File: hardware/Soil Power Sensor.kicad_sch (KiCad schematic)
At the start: 0 parts

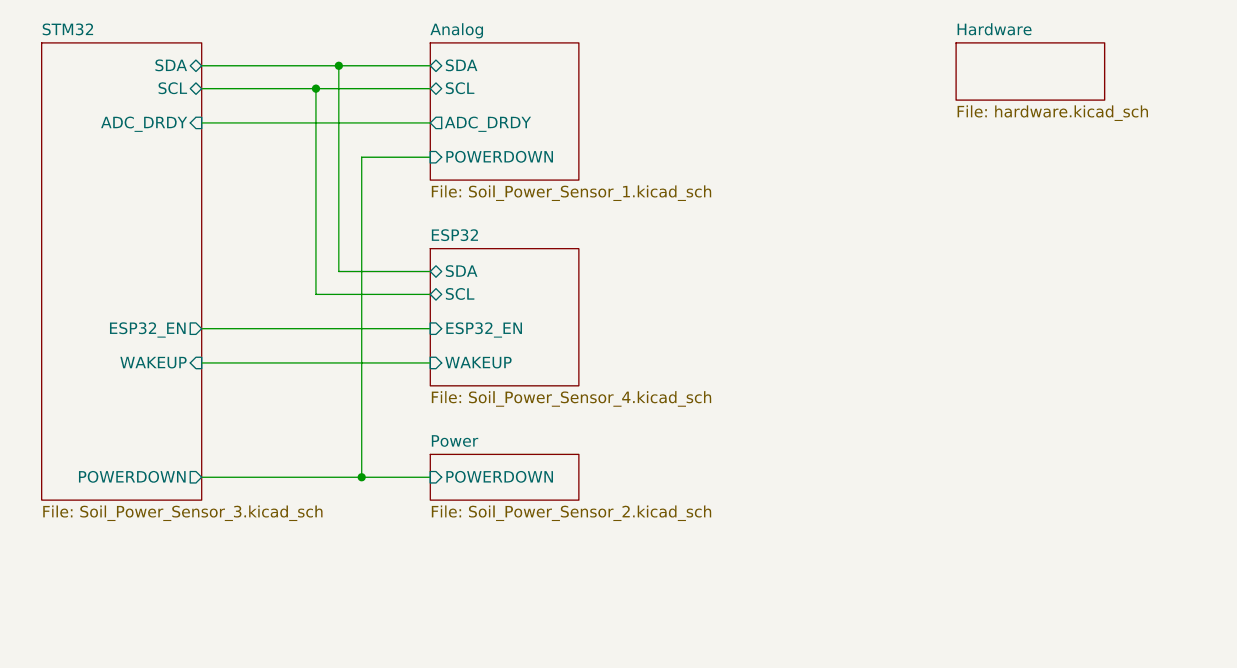
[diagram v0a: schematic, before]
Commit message: Fixed issues from design review
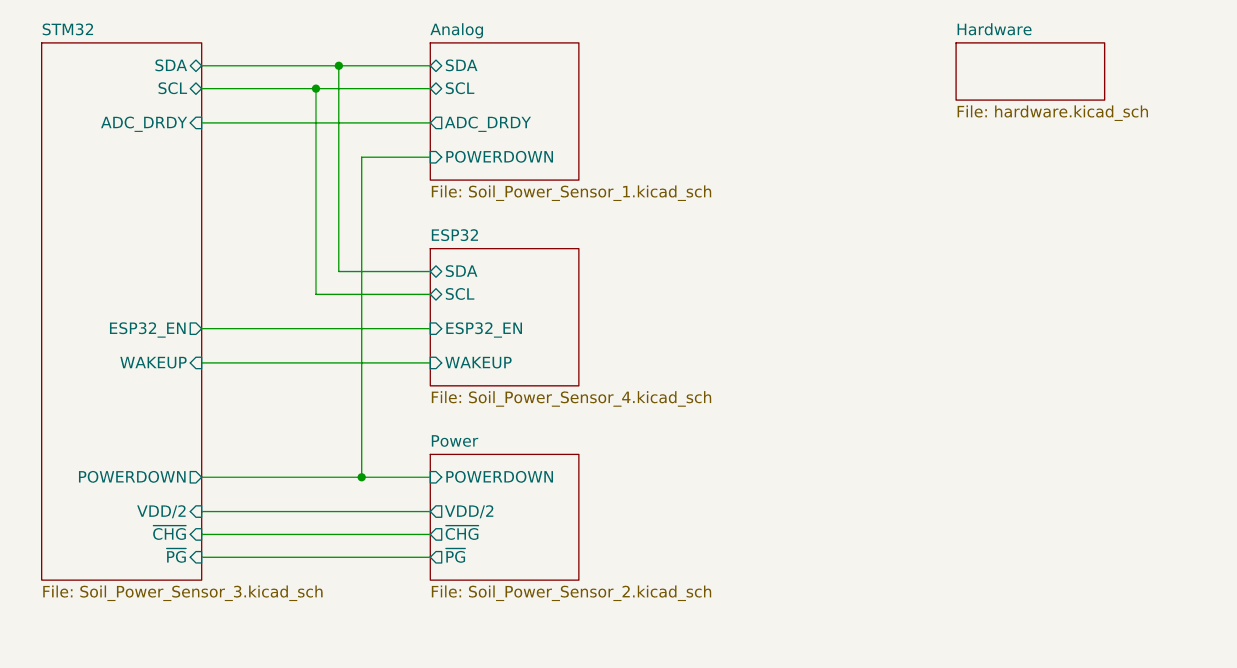
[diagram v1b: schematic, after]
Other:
- sheet Power ports: added VDD/2, ~{CHG}, ~{PG}; removed none
- sheet STM32 ports: added VDD/2, ~{CHG}, ~{PG}; removed none
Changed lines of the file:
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@@
+	(wire
+		(pts
+			(xy 137.16 129.54) (xy 162.56 129.54)
+		)
+		(stroke
+			(width 0)
+			(type default)
+		)
+	)
 	(wire
 		(pts
@@
 	(wire
 		(pts
+			(xy 137.16 127) (xy 162.56 127)
+		)
+		(stroke
+			(width 0)
+			(type default)
+		)
+	)
+	(wire
+		(pts
 			(xy 137.16 107.95) (xy 162.56 107.95)
+		)
+		(stroke
+			(width 0)
+			(type default)
+		)
+	)
+	(wire
+		(pts
+			(xy 137.16 124.46) (xy 162.56 124.46)
 		)
 		(stroke
@@
 	(sheet
 		(at 119.38 72.39)
-		(size 17.78 50.8)
+		(size 17.78 59.69)
 		(fields_autoplaced yes)
 		(stroke
@@
 		)
 		(property "Sheetfile" "Soil_Power_Sensor_3.kicad_sch"
-			(at 119.38 123.7746 0)
+			(at 119.38 132.6646 0)
 			(effects
 				(font
@@
 		(pin "WAKEUP" input
 			(at 137.16 107.95 0)
+			(effects
+				(font
+					(size 1.27 1.27)
+				)
+				(justify right)
+			)
+		)
+		(pin "~{PG}" input
+			(at 137.16 129.54 0)
+			(effects
+				(font
+					(size 1.27 1.27)
+				)
+				(justify right)
+			)
+		)
+		(pin "~{CHG}" input
+			(at 137.16 127 0)
+			(effects
+				(font
+					(size 1.27 1.27)
+				)
+				(justify right)
+			)
+		)
+		(pin "VDD{slash}2" input
+			(at 137.16 124.46 0)
 			(effects
 				(font
@@
 	(sheet
 		(at 162.56 118.11)
-		(size 16.51 5.08)
+		(size 16.51 13.97)
 		(fields_autoplaced yes)
 		(stroke
@@
 		)
 		(property "Sheetfile" "Soil_Power_Sensor_2.kicad_sch"
-			(at 162.56 123.7746 0)
+			(at 162.56 132.6646 0)
 			(effects
 				(font
@@
 			(effects
 				(font
+					(size 1.27 1.27)
+				)
+				(justify left)
+			)
+		)
+		(pin "~{CHG}" output
+			(at 162.56 127 180)
+			(effects
+				(font
+					(size 1.27 1.27)
+				)
+				(justify left)
+			)
+		)
+		(pin "~{PG}" output
+			(at 162.56 129.54 180)
+			(effects
+				(font
+					(size 1.27 1.27)
+				)
+				(justify left)
+			)
+		)
+		(pin "VDD{slash}2" output
+			(at 162.56 124.46 180)
+			(effects
+				(font

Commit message: Fixed issue with battery connector
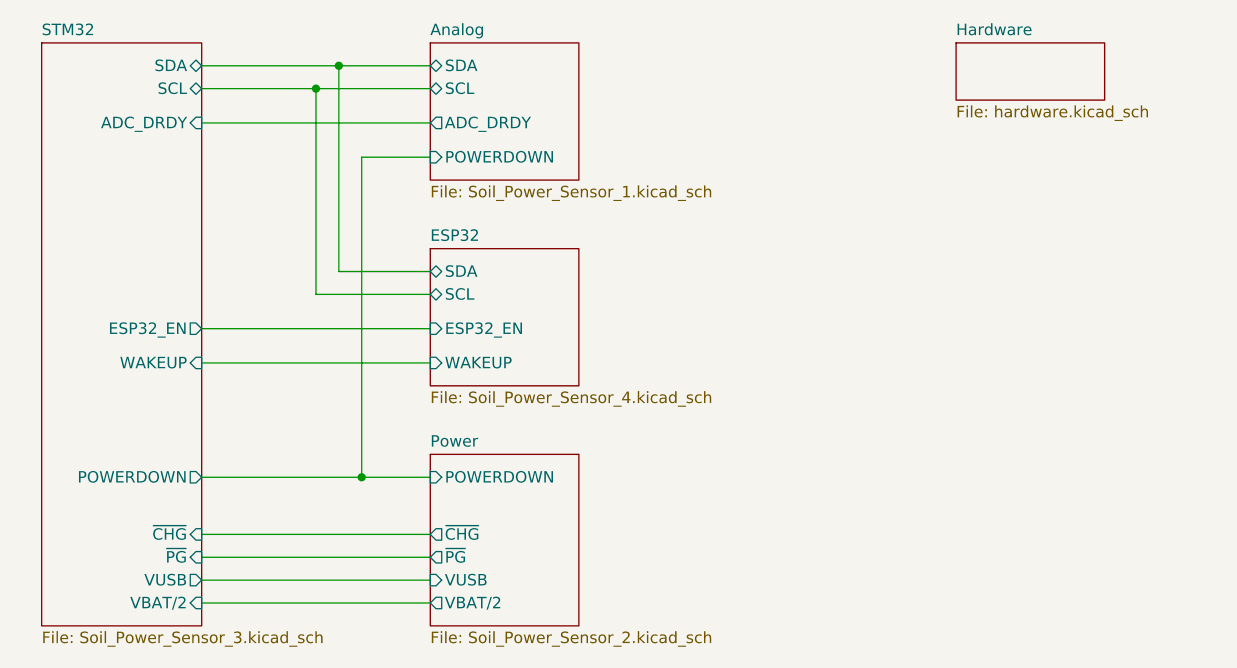
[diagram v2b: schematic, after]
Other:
- sheet Power ports: added VBAT/2, VUSB; removed VDD/2
- sheet STM32 ports: added VBAT/2, VUSB; removed VDD/2
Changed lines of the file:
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@@
-	(wire
-		(pts
-			(xy 137.16 124.46) (xy 162.56 124.46)
-		)
-		(stroke
-			(width 0)
-			(type default)
-		)
-	)
 	(wire
 		(pts
@@
 	(wire
 		(pts
+			(xy 137.16 134.62) (xy 162.56 134.62)
+		)
+		(stroke
+			(width 0)
+			(type default)
+		)
+	)
+	(wire
+		(pts
 			(xy 137.16 74.93) (xy 152.4 74.93)
 		)
@@
 		(pts
 			(xy 137.16 77.47) (xy 149.86 77.47)
+		)
+		(stroke
+			(width 0)
+			(type default)
+		)
+	)
+	(wire
+		(pts
+			(xy 137.16 132.08) (xy 162.56 132.08)
 		)
 		(stroke
@@
 	(sheet
 		(at 119.38 72.39)
-		(size 17.78 59.69)
+		(size 17.78 64.77)
 		(fields_autoplaced yes)
 		(stroke
@@
 		)
 		(property "Sheetfile" "Soil_Power_Sensor_3.kicad_sch"
-			(at 119.38 132.6646 0)
+			(at 119.38 137.7446 0)
 			(effects
 				(font
@@
 			)
 		)
-		(pin "VDD{slash}2" input
-			(at 137.16 124.46 0)
+		(pin "VUSB" output
+			(at 137.16 132.08 0)
+			(effects
+				(font
+					(size 1.27 1.27)
+				)
+				(justify right)
+			)
+		)
+		(pin "VBAT{slash}2" input
+			(at 137.16 134.62 0)
 			(effects
 				(font
@@
 	(sheet
 		(at 162.56 118.11)
-		(size 16.51 13.97)
+		(size 16.51 19.05)
 		(fields_autoplaced yes)
 		(stroke
@@
 		)
 		(property "Sheetfile" "Soil_Power_Sensor_2.kicad_sch"
-			(at 162.56 132.6646 0)
+			(at 162.56 137.7446 0)
 			(effects
 				(font
@@
 			)
 		)
-		(pin "VDD{slash}2" output
-			(at 162.56 124.46 180)
-			(effects
-				(font
+		(pin "VBAT{slash}2" output
+			(at 162.56 134.62 180)
+			(effects
+				(font
+					(size 1.27 1.27)
+				)
+				(justify left)
+			)
+		)
+		(pin "VUSB" input
+			(at 162.56 132.08 180)
+			(effects
+				(font

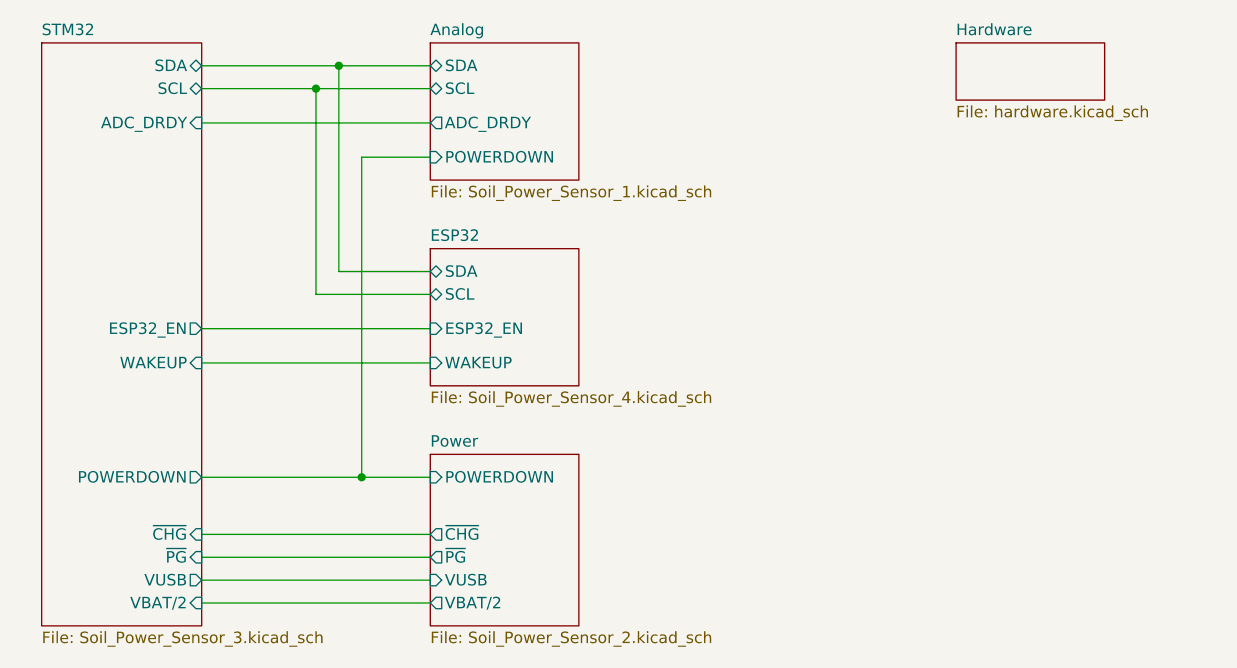
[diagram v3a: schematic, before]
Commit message: replace mini with module
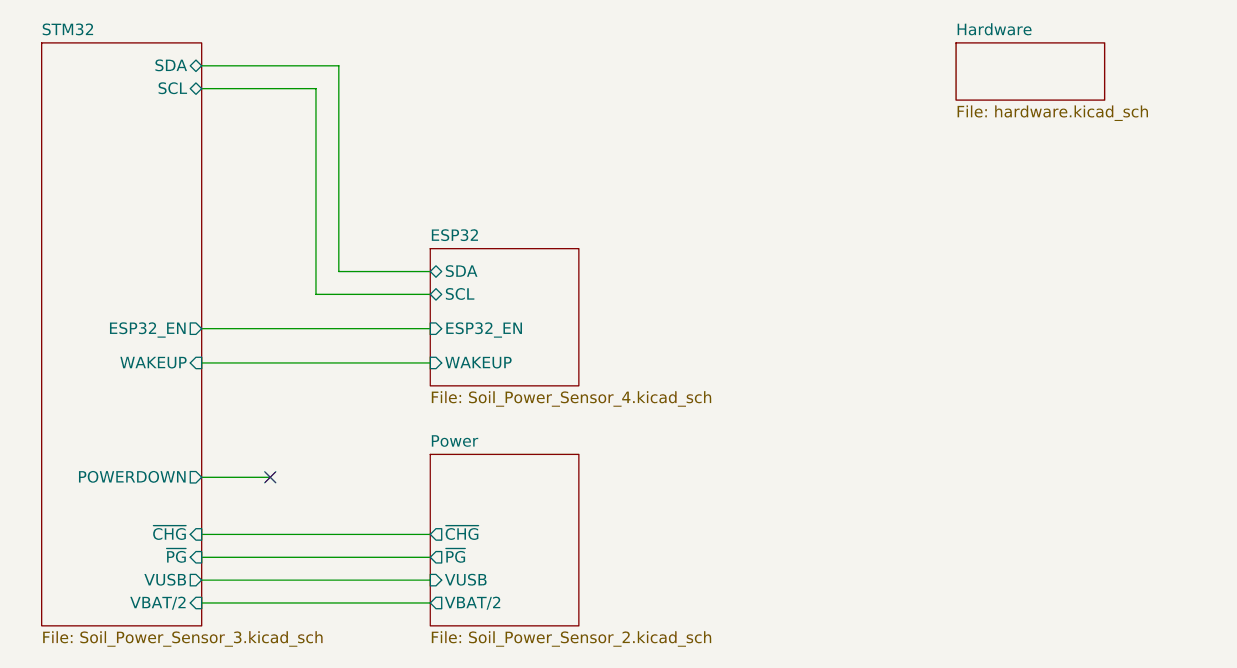
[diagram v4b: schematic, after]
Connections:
- no-connect marks 0 -> 1
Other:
- removed sheet Analog
- sheet Power ports: added none; removed POWERDOWN
- sheet STM32 ports: added none; removed ADC_DRDY
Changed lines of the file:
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@@
 (kicad_sch
-	(version 20231120)
+	(version 20250114)
 	(generator "eeschema")
-	(generator_version "8.0")
+	(generator_version "9.0")
 	(paper "A4")
 	(title_block
@@
 		(company "jlab")
 	)
-	(junction
-		(at 152.4 74.93)
-		(diameter 0)
-		(color 0 0 0 0)
-	)
-	(junction
-		(at 149.86 77.47)
-		(diameter 0)
-		(color 0 0 0 0)
-	)
-	(junction
-		(at 154.94 120.65)
-		(diameter 0)
-		(color 0 0 0 0)
-	)
-	(wire
-		(pts
-			(xy 137.16 81.28) (xy 162.56 81.28)
-		)
-		(stroke
-			(width 0)
-			(type default)
-		)
+	(no_connect
+		(at 144.78 120.65)
 	)
 	(wire
@@
 	(wire
 		(pts
-			(xy 149.86 77.47) (xy 162.56 77.47)
-		)
-		(stroke
-			(width 0)
-			(type default)
-		)
-	)
-	(wire
-		(pts
 			(xy 137.16 127) (xy 162.56 127)
 		)
@@
 	(wire
 		(pts
+			(xy 137.16 120.65) (xy 144.78 120.65)
+		)
+		(stroke
+			(width 0)
+			(type default)
+		)
+	)
+	(wire
+		(pts
 			(xy 162.56 100.33) (xy 149.86 100.33)
 		)
@@
 	(wire
 		(pts
-			(xy 154.94 85.09) (xy 154.94 120.65)
-		)
-		(stroke
-			(width 0)
-			(type default)
-		)
-	)
-	(wire
-		(pts
-			(xy 152.4 74.93) (xy 162.56 74.93)
-		)
-		(stroke
-			(width 0)
-			(type default)
-		)
-	)
-	(wire
-		(pts
 			(xy 137.16 134.62) (xy 162.56 134.62)
 		)
@@
 	(wire
 		(pts
-			(xy 162.56 85.09) (xy 154.94 85.09)
-		)
-		(stroke
-			(width 0)
-			(type default)
-		)
-	)
-	(wire
-		(pts
 			(xy 137.16 77.47) (xy 149.86 77.47)
 		)
@@
 	(wire
 		(pts
-			(xy 154.94 120.65) (xy 162.56 120.65)
-		)
-		(stroke
-			(width 0)
-			(type default)
-		)
-	)
-	(wire
-		(pts
 			(xy 149.86 77.47) (xy 149.86 100.33)
 		)
@@
 		(pts
 			(xy 152.4 74.93) (xy 152.4 97.79)
-		)
-		(stroke
-			(width 0)
-			(type default)
-		)
-	)
-	(wire
-		(pts
-			(xy 137.16 120.65) (xy 154.94 120.65)
 		)
 		(stroke
@@
 		(at 162.56 95.25)
 		(size 16.51 15.24)
+		(exclude_from_sim no)
+		(in_bom yes)
+		(on_board yes)
+		(dnp no)
 		(fields_autoplaced yes)
 		(stroke
@@
 		(at 119.38 72.39)
 		(size 17.78 64.77)
+		(exclude_from_sim no)
+		(in_bom yes)
+		(on_board yes)
+		(dnp no)
 		(fields_autoplaced yes)
 		(stroke
@@
 		(pin "ESP32_EN" output
 			(at 137.16 104.14 0)
-			(effects
-				(font
-					(size 1.27 1.27)
-				)
-				(justify right)
-			)
-		)
-		(pin "ADC_DRDY" input
-			(at 137.16 81.28 0)
 			(effects
 				(font
@@
 		(at 162.56 118.11)
 		(size 16.51 19.05)
+		(exclude_from_sim no)
+		(in_bom yes)
+		(on_board yes)
+		(dnp no)
 		(fields_autoplaced yes)
 		(stroke
@@
 				)
 				(justify left top)
-			)
-		)
-		(pin "POWERDOWN" input
-			(at 162.56 120.65 180)
-			(effects
-				(font
-					(size 1.27 1.27)
-				)
-				(justify left)
 			)
 		)
@@
 	)
 	(sheet
-		(at 162.56 72.39)
-		(size 16.51 15.24)
-		(fields_autoplaced yes)
-		(stroke
-			(width 0)
-			(type solid)
-		)
-		(fill
-			(color 0 0 0 0.0000)
-		)
-		(property "Sheetname" "Analog"
-			(at 162.56 71.6784 0)
-			(effects
-				(font
-					(size 1.27 1.27)
-				)
-				(justify left bottom)
-			)
-		)
-		(property "Sheetfile" "Soil_Power_Sensor_1.kicad_sch"
-			(at 162.56 88.2146 0)
-			(effects
-				(font
-					(size 1.27 1.27)
-				)
-				(justify left top)
-			)
-		)
-		(pin "ADC_DRDY" output
-			(at 162.56 81.28 180)
-			(effects
-				(font
-					(size 1.27 1.27)
-				)
-				(justify left)
-			)
-		)
-		(pin "SCL" bidirectional
-			(at 162.56 77.47 180)
-			(effects
-				(font
-					(size 1.27 1.27)
-				)
-				(justify left)
-			)
-		)
-		(pin "SDA" bidirectional
-			(at 162.56 74.93 180)
-			(effects
-				(font
-					(size 1.27 1.27)
-				)
-				(justify left)
-			)
-		)
-		(pin "POWERDOWN" input
-			(at 162.56 85.09 180)
-			(effects
-				(font
-					(size 1.27 1.27)
-				)
-				(justify left)
-			)
-		)
-		(instances
-			(project "Soil Power Sensor"
-				(path "/5300ec4d-4648-40a1-8d89-4fa6b3bf32a3"
-					(page "1")
-				)
-			)
-		)
-	)
-	(sheet
 		(at 220.98 72.39)
 		(size 16.51 6.35)
+		(exclude_from_sim no)
+		(in_bom yes)
+		(on_board yes)
+		(dnp no)
 		(fields_autoplaced yes)
 		(stroke
@@
 		)
 	)
+	(embedded_fonts no)
 )

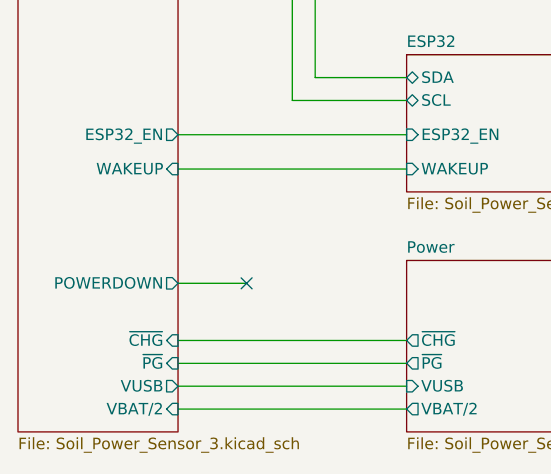
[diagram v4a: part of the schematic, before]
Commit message: pin numbering and changed mosfets
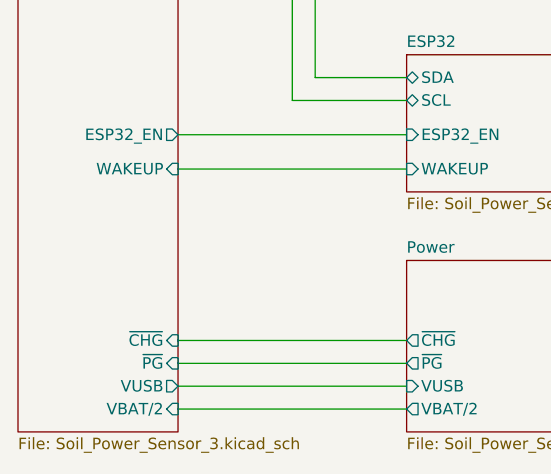
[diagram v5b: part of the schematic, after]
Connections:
- no-connect marks 1 -> 0
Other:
- sheet STM32 ports: added none; removed POWERDOWN
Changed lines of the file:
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@@
 		(company "jlab")
 	)
-	(no_connect
-		(at 144.78 120.65)
-	)
 	(wire
 		(pts
@@
 		(pts
 			(xy 137.16 107.95) (xy 162.56 107.95)
-		)
-		(stroke
-			(width 0)
-			(type default)
-		)
-	)
-	(wire
-		(pts
-			(xy 137.16 120.65) (xy 144.78 120.65)
 		)
 		(stroke
@@
 			(effects
 				(font
-					(size 1.27 1.27)
-				)
-				(justify right)
-			)
-		)
-		(pin "POWERDOWN" output
-			(at 137.16 120.65 0)
-			(effects
-				(font
